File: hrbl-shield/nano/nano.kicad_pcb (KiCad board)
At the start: 2 copper layers, 96.8 x 140.1 mm, 56 parts, among them P1 Digital, P2 Analog, P3 CONN_01X01, P4 CONN_01X01, P5 CONN_01X01, P6 CONN_01X01, U1 SFH6206-3T, U10 SFH6206-3T, U11 SFH6206-3T, U12 SFH6206-3T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

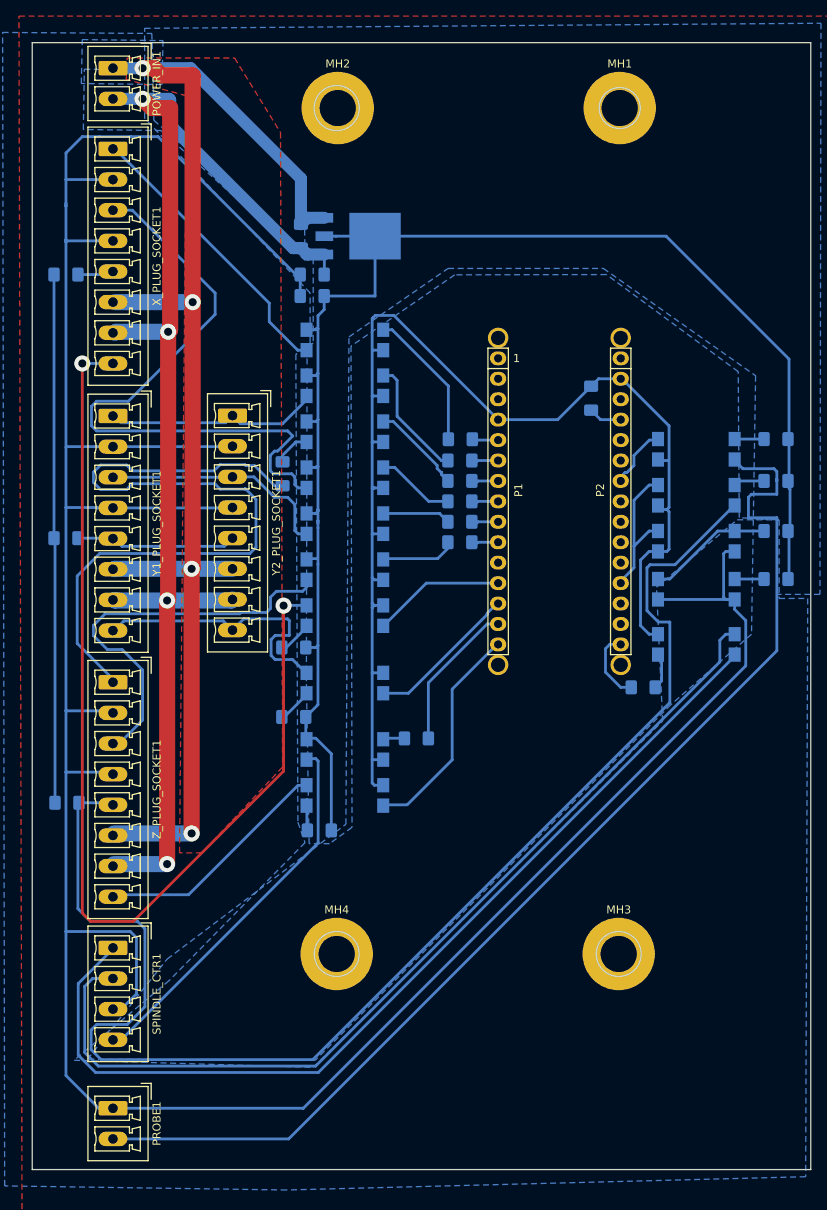
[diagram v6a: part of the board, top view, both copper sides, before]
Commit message: nano sheild and manual
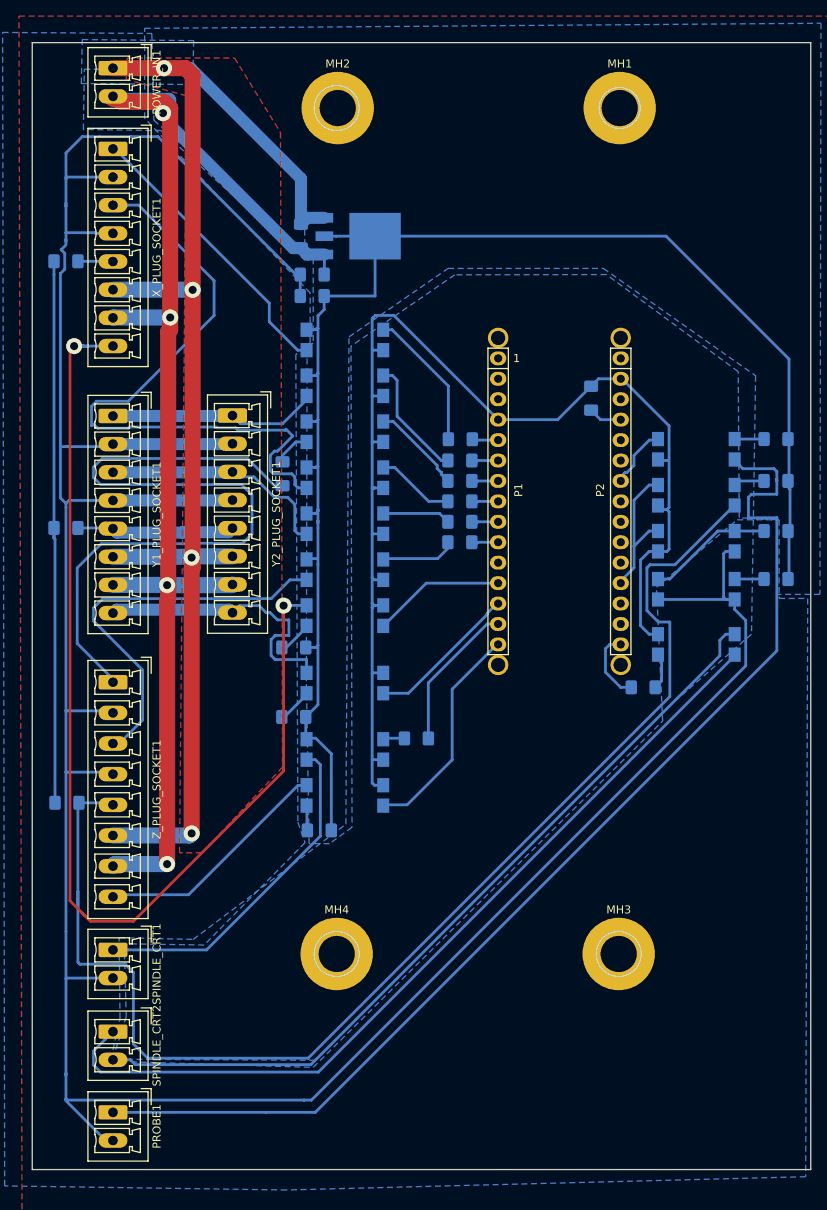
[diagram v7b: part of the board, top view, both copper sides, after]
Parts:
- removed SPINDLE_CTR1: Conn_01x04, Connector_Phoenix_MC:PhoenixContact_MCV_1,5_4-G-3.81_1x04_P3.81mm_Vertical
- added SPINDLE_CRT1: Conn_01x02, Connector_Phoenix_MC:PhoenixContact_MCV_1,5_2-G-3.5_1x02_P3.50mm_Vertical, F.Cu at (91.6, 144.8)
- added SPINDLE_CRT2: Conn_01x02, Connector_Phoenix_MC:PhoenixContact_MCV_1,5_2-G-3.5_1x02_P3.50mm_Vertical, F.Cu at (91.6, 154.9)
- POWER_IN1, PROBE1: footprint Connector_Phoenix_MC:PhoenixContact_MCV_1,5_2-G-3.81_1x02_P3.81mm_Vertical -> Connector_Phoenix_MC:PhoenixContact_MCV_1,5_2-G-3.5_1x02_P3.50mm_Vertical
- X_PLUG_SOCKET1, Y1_PLUG_SOCKET1, Y2_PLUG_SOCKET1: footprint Connector_Phoenix_MC:PhoenixContact_MCV_1,5_8-G-3.81_1x08_P3.81mm_Vertical -> Connector_Phoenix_MC:PhoenixContact_MCV_1,5_8-G-3.5_1x08_P3.50mm_Vertical
- moved R16 1.65 mm to (85.7, 59.2)
- moved R17 1.27 mm to (85.7, 92.3)
- moved PROBE1 0.51 mm to (91.6, 165.0)
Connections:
- PROBE1 pad 1: GNDS -> /PROBE_PLATE
- PROBE1 pad 2: /PROBE_PLATE -> GNDS
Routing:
- net /SPINDLE_EN_OUT: track 117.6 -> 100.8 mm
- net +36V: track 190.9 -> 177.0 mm
- net /+24V_IN: track 119.3 -> 106.8 mm
- net ALARM_IN: track 260.5 -> 252.8 mm
- net LIM_X_IN: track 129.0 -> 135.8 mm
- net GNDPWR: track 176.5 -> 170.0 mm
- net /SPINDLE_PWM_OUT: track 47.2 -> 42.5 mm
- net GNDS: track 377.7 -> 374.2 mm
- net DIR_X_OUT: track 79.1 -> 82.3 mm
- net PUL_Z_OUT: track 93.1 -> 91.4 mm
- net /PROBE_PLATE: track 142.9 -> 141.7 mm
- net LIM_Y_IN: track 35.0 -> 36.3 mm
- net PUL_Y_OUT: track 28.2 -> 27.6 mm

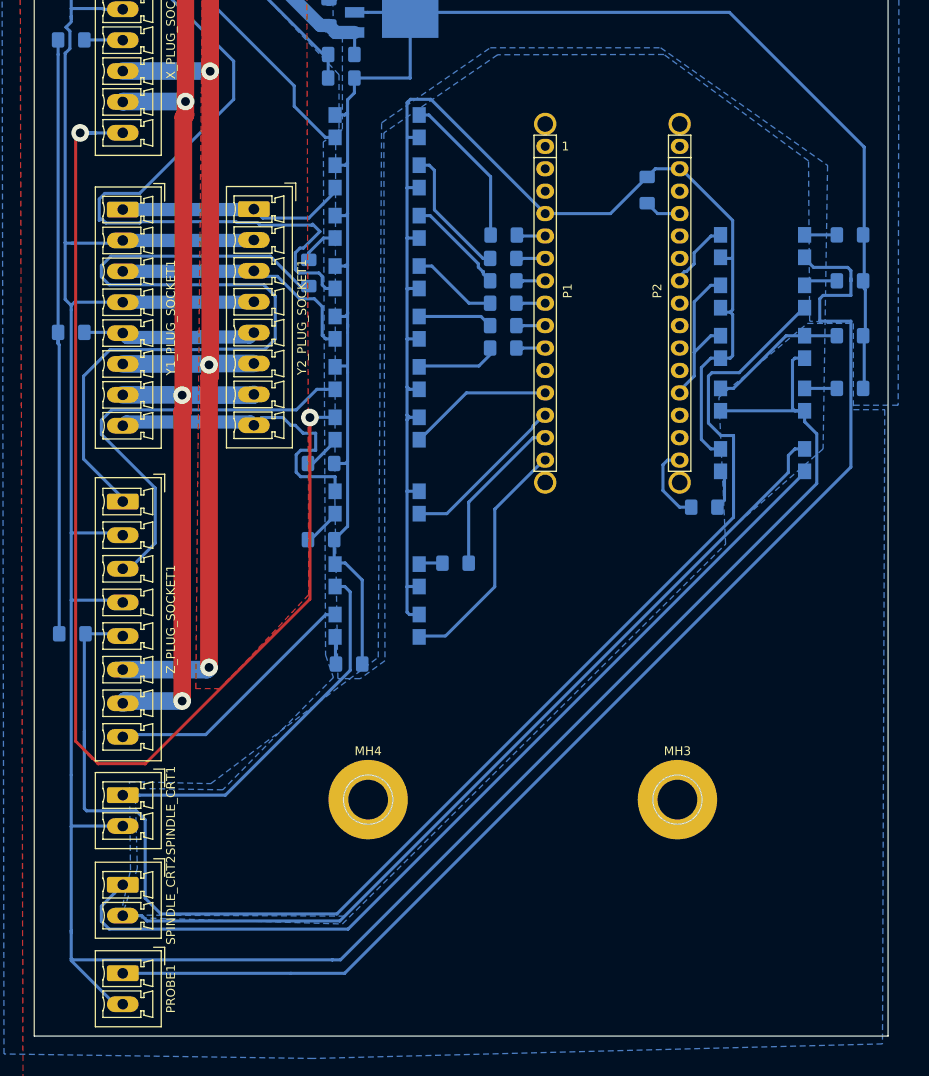
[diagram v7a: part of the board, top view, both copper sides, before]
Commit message: Dust skirt
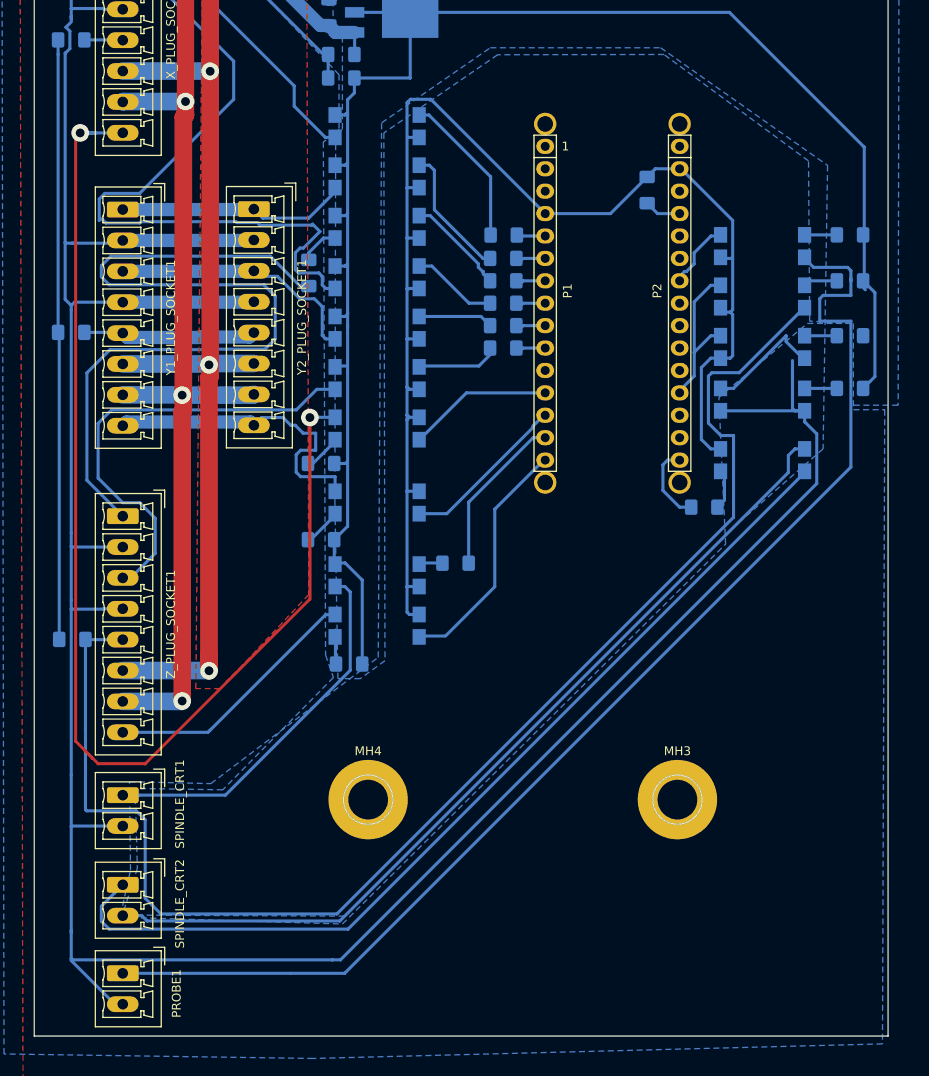
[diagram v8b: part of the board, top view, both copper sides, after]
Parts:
- Z_PLUG_SOCKET1: footprint Connector_Phoenix_MC:PhoenixContact_MCV_1,5_8-G-3.81_1x08_P3.81mm_Vertical -> Connector_Phoenix_MC:PhoenixContact_MCV_1,5_8-G-3.5_1x08_P3.50mm_Vertical
- moved Z_PLUG_SOCKET1 1.65 mm to (91.6, 113.2)
- moved R18 0.63 mm to (85.9, 127.1)
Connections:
- net Net-(R2-Pad1) renamed /DIODE3
- net Net-(R3-Pad1) renamed /DIODE2
- net Net-(R4-Pad1) renamed /DIODE
- R15 pad 2: 5V_ISO -> +5V
- U1 pad 4: /PWR_SIG -> /PWR_ABR
- U2 pad 2: GNDS -> /PWR_ABR
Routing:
- net /PWR_ABR: track 0.00 -> 13.4 mm
- net /PWR_SIG: track 15.8 -> 3.78 mm
- net ALARM_IN: track 252.8 -> 249.9 mm
- net DIR_Z_OUT: track 49.1 -> 51.8 mm
- net 5V_ISO: track 184.5 -> 186.6 mm
- net GNDS: track 374.2 -> 372.5 mm
- net +36V: track 177.0 -> 178.7 mm
- net PUL_Z_OUT: track 91.4 -> 93.0 mm
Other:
- board text added: "CUT AND MOVE"
- board text added: "CUT FREE AND LINK TO 5V"
